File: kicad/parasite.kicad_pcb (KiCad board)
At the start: 2 copper layers, 22 x 126.4 mm, 31 parts, among them Q1 MMBT3906, Q4 Q_Photo_NPN, SW1 B3U-1000P, U1 E73-2G4M08S1C, U2 SHTC3, Y1 32.768kHz

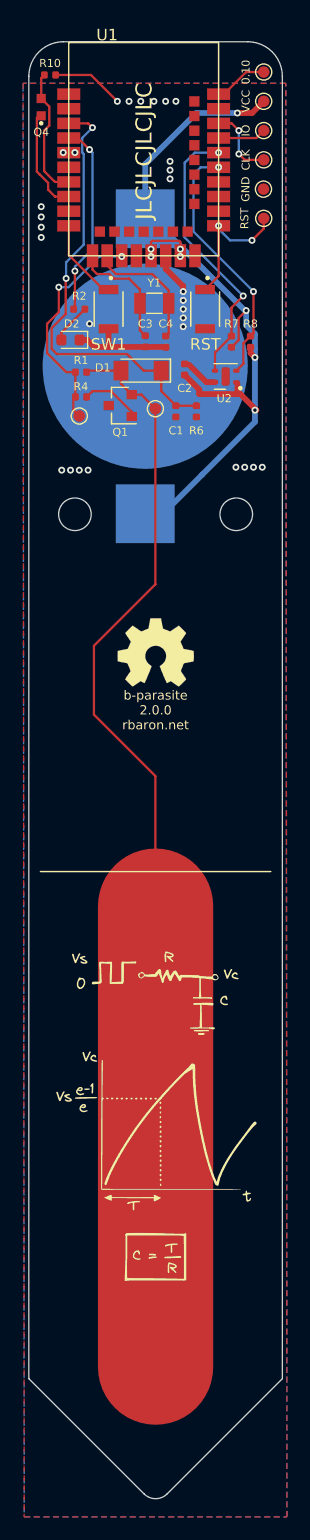
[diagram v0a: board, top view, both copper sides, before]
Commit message: Javított nyák, más méretű optó tranzisztor (0806)
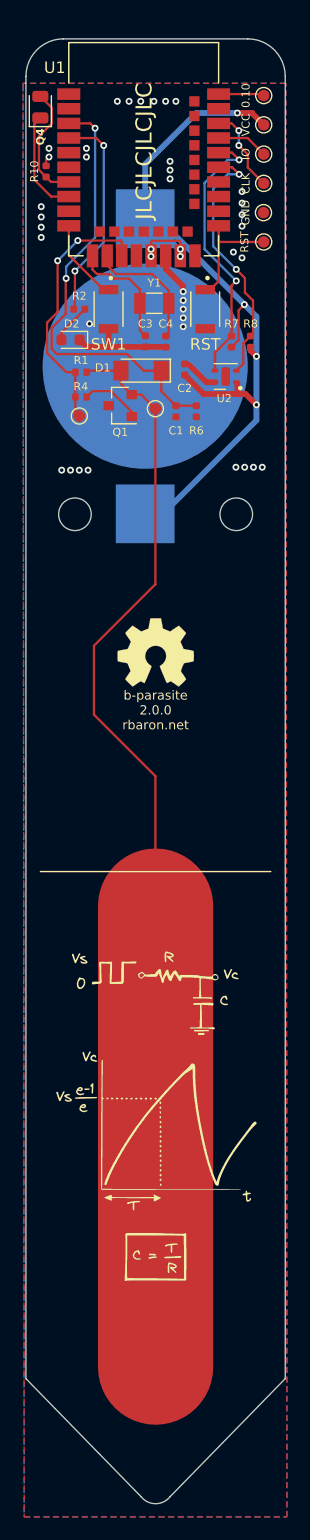
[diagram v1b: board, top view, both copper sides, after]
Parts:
- Q4: footprint snapeda:TR8 -> LED_SMD:LED_0805_2012Metric
- moved R10 8.37 mm to (58.5, 38.2), turned to -90 degrees
- moved TP1 2.04 mm to (77.4, 36.8)
- moved TP2 2.04 mm to (77.4, 39.3)
- moved TP3 2.04 mm to (77.4, 41.8)
- moved TP7 2.04 mm to (77.4, 34.2)
- moved TP8 2.04 mm to (77.4, 31.7)
- moved TP4 2.04 mm to (77.4, 44.4)
- moved Q4 0.08 mm to (58.0, 32.7)
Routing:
- net GND: track 22.2 -> 16.8 mm, vias 29 -> 37
- net PWM: track 20.1 -> 23.0 mm
- net LED: track 16.9 -> 18.6 mm
- net RST: track 11.9 -> 10.2 mm, vias 2 -> 0
- net PHOTO_OUT: track 11.5 -> 10.3 mm
- net SWDCLK: track 6.42 -> 7.49 mm
- net 0.10: track 4.71 -> 3.97 mm
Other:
- board size 22 x 126.4 mm -> 22.5 x 127.1 mm
- rule pad_to_mask_clearance: 0.051 -> 0.05
